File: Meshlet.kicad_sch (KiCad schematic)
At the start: 99 parts, among them J11 GPIO Exp., J12 GPS Header, J13 Thermistor Pins, J14 Ext. Notif. Header, J2 User Btn Header, J3 Batt. Header (Picoblade 1.25), J4 Batt. Header (JST-PH 2.0), J5 USB_C_Receptacle_USB2.0_16P, J6 STEMMA QT I2C, J7 Ext. Power Header, J9 Ext. Power Header, Q1 AO3400A, SW2 BOOTSEL, U1 XC6206PxxxMR, U11 INA3221, U2 USBLC6-2SC6, U3 XC6206PxxxMR, U4 RP2350_60QFN, U5 Wio-SX1262, U6 BQ25185, U7 BME280, U8 W25Q32JVZP, U9 XC6206PxxxMR, Y1 12.000MHz

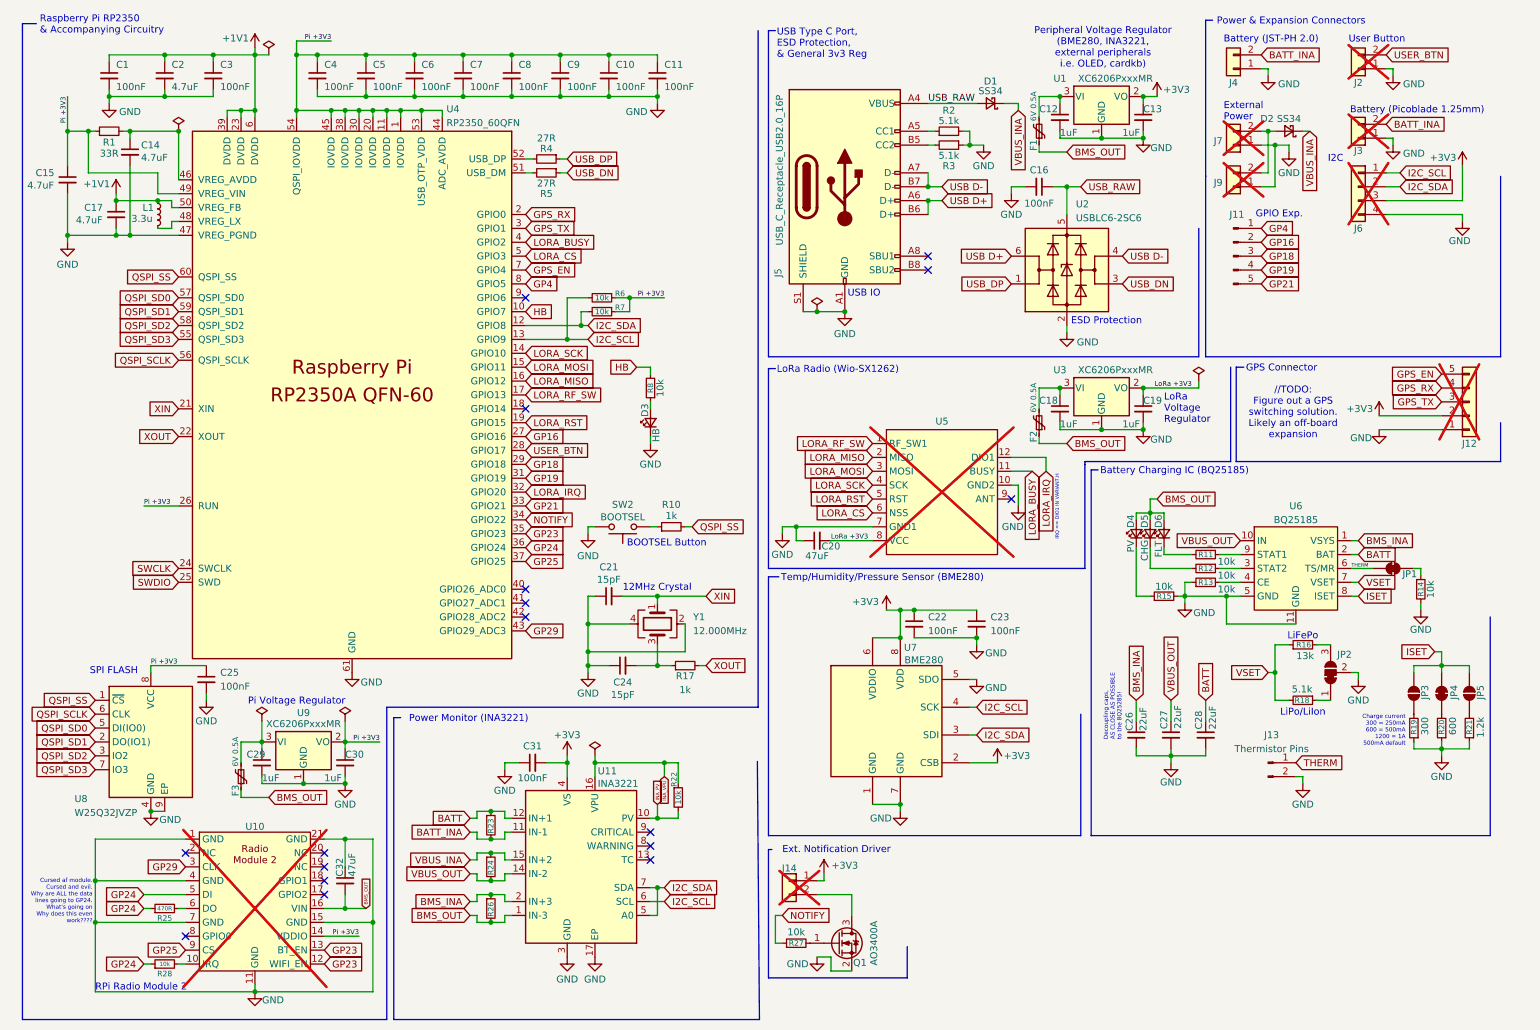
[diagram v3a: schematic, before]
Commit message: Add GPS header
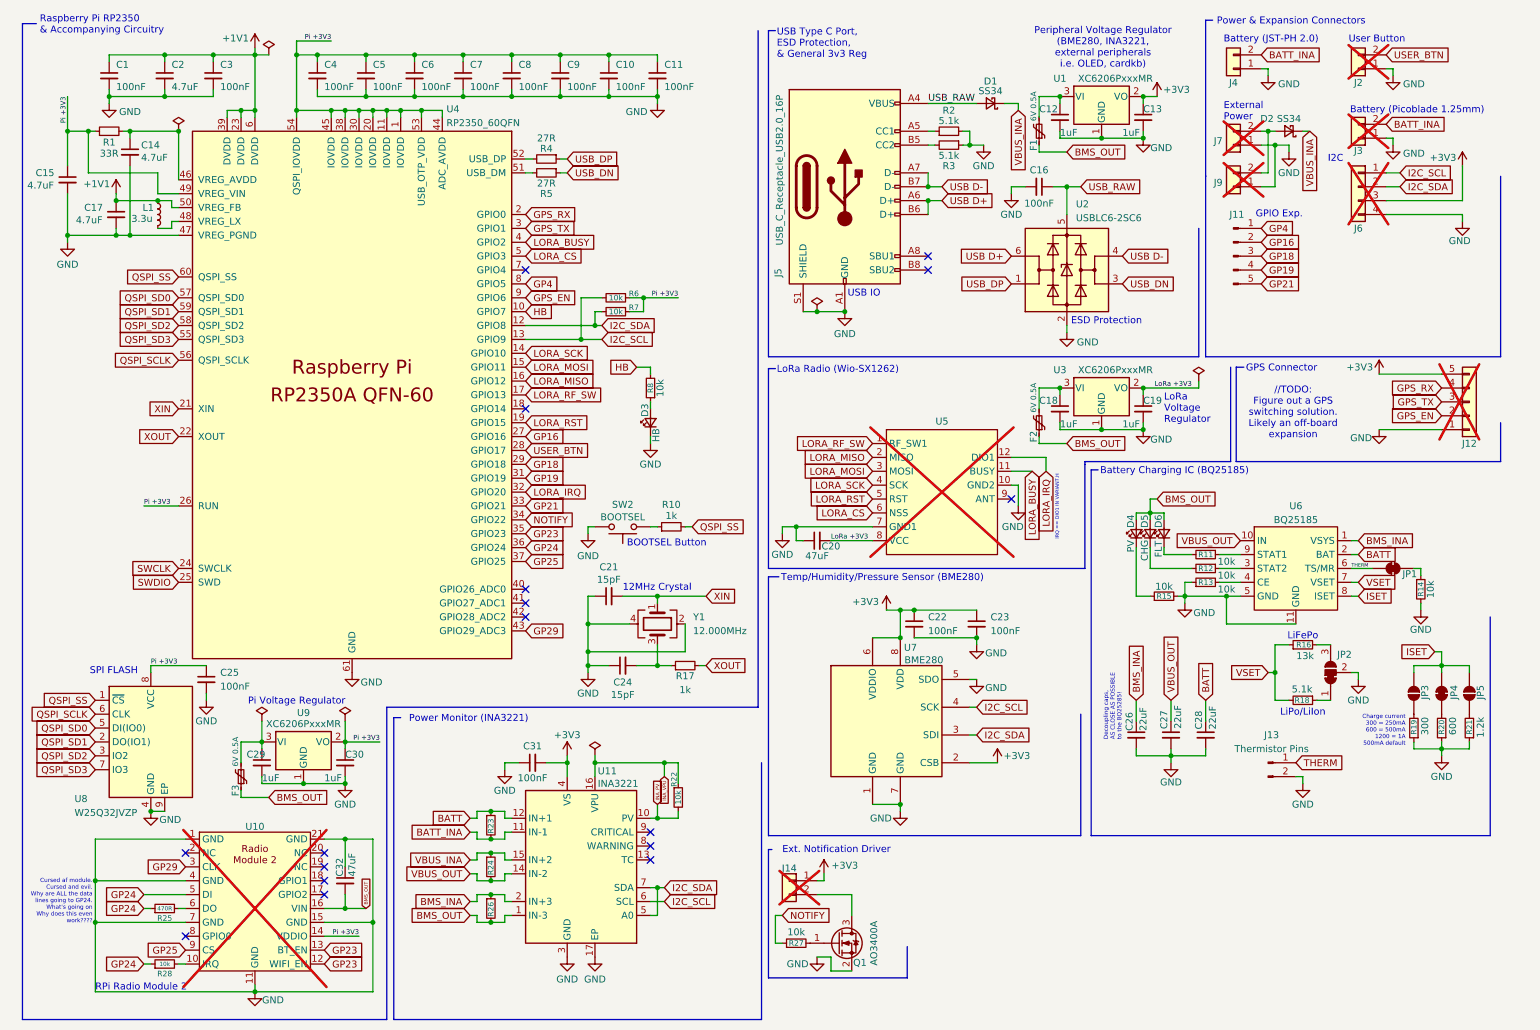
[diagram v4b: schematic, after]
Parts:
- J12: footprint Connector_PinHeader_2.00mm:PinHeader_1x05_P2.00mm_Vertical -> Connector_PinHeader_1.27mm:PinHeader_1x05_P1.27mm_Vertical
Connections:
- net +3V3: now also J12.5 (Pin_5); no longer J12.2 (Pin_2)
- net GPS_EN: now also J12.2 (Pin_2), U4.9 (GPIO6); no longer J12.5 (Pin_5), U4.7 (GPIO4)
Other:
- moved on the sheet: R6, R7
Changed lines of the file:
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@@
 	)
 	(junction
+		(at 118.11 69.85)
+		(diameter 0)
+		(color 0 0 0 0)
+	)
+	(junction
 		(at 21.59 34.29)
 		(diameter 0)
@@
 	)
 	(junction
-		(at 115.57 69.85)
-		(diameter 0)
-		(color 0 0 0 0)
-	)
-	(junction
 		(at 210.82 88.9)
 		(diameter 0)
@@
 	)
 	(junction
-		(at 124.46 64.77)
+		(at 127 64.77)
 		(diameter 0)
 		(color 0 0 0 0)
@@
 	)
 	(junction
+		(at 115.57 72.39)
+		(diameter 0)
+		(color 0 0 0 0)
+	)
+	(junction
 		(at 39.37 20.32)
 		(diameter 0)
@@
 		(color 0 0 0 0)
 	)
-	(junction
-		(at 113.03 72.39)
-		(diameter 0)
-		(color 0 0 0 0)
-	)
 	(no_connect
 		(at 105.41 123.19)
 	)
 	(no_connect
-		(at 105.41 64.77)
-	)
-	(no_connect
 		(at 105.41 118.11)
 	)
@@
 	)
 	(no_connect
+		(at 105.41 59.69)
+	)
+	(no_connect
 		(at 43.18 181.61)
 	)
@@
 	(wire
 		(pts
-			(xy 115.57 69.85) (xy 116.84 69.85)
-		)
-		(stroke
-			(width 0)
-			(type default)
-		)
-	)
-	(wire
-		(pts
-			(xy 105.41 72.39) (xy 113.03 72.39)
+			(xy 105.41 72.39) (xy 115.57 72.39)
 		)
 		(stroke
@@
 	(polyline
 		(pts
-			(xy 147.828 149.606) (xy 148.209 196.85)
+			(xy 148.59 149.86) (xy 148.59 196.85)
 		)
 		(stroke
@@
 		)
 	)
+	(wire
+		(pts
+			(xy 115.57 72.39) (xy 119.38 72.39)
+		)
+		(stroke
+			(width 0)
+			(type default)
+		)
+	)
 	(polyline
 		(pts
@@
 	(wire
 		(pts
-			(xy 121.92 67.31) (xy 124.46 67.31)
+			(xy 124.46 67.31) (xy 127 67.31)
 		)
 		(stroke
@@
 	(wire
 		(pts
-			(xy 261.62 86.36) (xy 273.05 86.36)
+			(xy 261.62 78.74) (xy 273.05 78.74)
 		)
 		(stroke
@@
 	(wire
 		(pts
-			(xy 105.41 69.85) (xy 115.57 69.85)
+			(xy 105.41 69.85) (xy 118.11 69.85)
 		)
 		(stroke
@@
 	(wire
 		(pts
-			(xy 116.84 67.31) (xy 115.57 67.31)
+			(xy 119.38 67.31) (xy 118.11 67.31)
 		)
 		(stroke
@@
 	(wire
 		(pts
-			(xy 115.57 67.31) (xy 115.57 69.85)
+			(xy 118.11 67.31) (xy 118.11 69.85)
 		)
 		(stroke
@@
 	(wire
 		(pts
-			(xy 116.84 64.77) (xy 113.03 64.77)
+			(xy 119.38 64.77) (xy 115.57 64.77)
 		)
 		(stroke
@@
 	(wire
 		(pts
+			(xy 118.11 69.85) (xy 119.38 69.85)
+		)
+		(stroke
+			(width 0)
+			(type default)
+		)
+	)
+	(wire
+		(pts
 			(xy 176.53 127) (xy 187.96 127)
 		)
@@
 	(wire
 		(pts
-			(xy 124.46 64.77) (xy 130.81 64.77)
+			(xy 127 64.77) (xy 133.35 64.77)
 		)
 		(stroke
@@
 	(wire
 		(pts
-			(xy 121.92 64.77) (xy 124.46 64.77)
+			(xy 124.46 64.77) (xy 127 64.77)
 		)
 		(stroke
@@
 	(polyline
 		(pts
-			(xy 81.28 196.85) (xy 148.209 196.85)
+			(xy 81.28 196.85) (xy 148.59 196.85)
 		)
 		(stroke
@@
 	(wire
 		(pts
-			(xy 124.46 67.31) (xy 124.46 64.77)
+			(xy 127 67.31) (xy 127 64.77)
 		)
 		(stroke
@@
 	(wire
 		(pts
-			(xy 113.03 64.77) (xy 113.03 72.39)
+			(xy 115.57 64.77) (xy 115.57 72.39)
 		)
 		(stroke
@@
 	(wire
 		(pts
-			(xy 113.03 72.39) (xy 116.84 72.39)
-		)
-		(stroke
-			(width 0)
-			(type default)
-		)
-	)
-	(wire
-		(pts
 			(xy 99.06 173.99) (xy 101.6 173.99)
 		)
@@
 	)
 	(label "Pi +3V3"
-		(at 130.81 64.77 180)
+		(at 133.35 64.77 180)
 		(effects
 			(font
@@
 	(global_label "GPS_EN"
 		(shape input)
-		(at 273.05 78.74 180)
+		(at 273.05 86.36 180)
 		(fields_autoplaced yes)
 		(effects
@@
 		)
 		(property "Intersheetrefs" "${INTERSHEET_REFS}"
-			(at 262.8682 78.74 0)
+			(at 262.8682 86.36 0)
 			(effects
 				(font
@@
 	(global_label "I2C_SDA"
 		(shape input)
-		(at 116.84 69.85 0)
+		(at 119.38 69.85 0)
 		(fields_autoplaced yes)
 		(effects
@@
 		)
 		(property "Intersheetrefs" "${INTERSHEET_REFS}"
-			(at 127.4452 69.85 0)
+			(at 129.9852 69.85 0)
 			(effects
 				(font
@@
 	(global_label "I2C_SCL"
 		(shape input)
-		(at 116.84 72.39 0)
+		(at 119.38 72.39 0)
 		(fields_autoplaced yes)
 		(effects
@@
 		)
 		(property "Intersheetrefs" "${INTERSHEET_REFS}"
-			(at 127.3847 72.39 0)
+			(at 129.9247 72.39 0)
 			(effects
 				(font
@@
 	(global_label "GPS_EN"
 		(shape input)
-		(at 105.41 59.69 0)
+		(at 105.41 64.77 0)
 		(fields_autoplaced yes)
 		(effects
@@
 		)
 		(property "Intersheetrefs" "${INTERSHEET_REFS}"
-			(at 112.1447 59.69 0)
+			(at 112.1447 64.77 0)
 			(effects
 				(font
@@
 			)
 		)
-		(property "Footprint" "Connector_PinHeader_2.00mm:PinHeader_1x05_P2.00mm_Vertical"
+		(property "Footprint" "Connector_PinHeader_1.27mm:PinHeader_1x05_P1.27mm_Vertical"
 			(at 278.13 83.82 0)
 			(effects
@@
 		(lib_name "R_Small_6")
 		(lib_id "Device:R_Small")
-		(at 119.38 67.31 270)
+		(at 121.92 67.31 270)
 		(unit 1)
 		(exclude_from_sim no)
@@
 		(dnp no)
 		(property "Reference" "R7"
-			(at 122.682 66.548 90)
+			(at 125.222 66.548 90)
 			(effects
 				(font
@@
 		)
 		(property "Value" "10k"
-			(at 119.38 67.31 90)
+			(at 121.92 67.31 90)
 			(effects
 				(font
@@
 		)
 		(property "Footprint" "Resistor_SMD:R_0402_1005Metric"
-			(at 119.38 67.31 0)
+			(at 121.92 67.31 0)
 			(effects
 				(font
@@
 		)
 		(property "Datasheet" "~"
-			(at 119.38 67.31 0)
+			(at 121.92 67.31 0)
 			(effects
 				(font
@@
 		)
 		(property "Description" "Resistor, small symbol"
-			(at 119.38 67.31 0)
+			(at 121.92 67.31 0)
 			(effects
 				(font
@@
 		)
 		(property "LCSC" "C25744"
-			(at 119.38 67.31 90)
+			(at 121.92 67.31 90)
 			(effects
 				(font
@@
 		(lib_name "R_Small_6")
 		(lib_id "Device:R_Small")
-		(at 119.38 64.77 270)
+		(at 121.92 64.77 270)
 		(unit 1)
 		(exclude_from_sim no)
@@
 		(dnp no)
 		(property "Reference" "R6"
-			(at 122.682 64.008 90)
+			(at 125.222 64.008 90)
 			(effects
 				(font
@@
 		)
 		(property "Value" "10k"
-			(at 119.38 64.77 90)
+			(at 121.92 64.77 90)
 			(effects
 				(font
@@
 		)
 		(property "Footprint" "Resistor_SMD:R_0402_1005Metric"
-			(at 119.38 64.77 0)
+			(at 121.92 64.77 0)
 			(effects
 				(font
@@
 		)
 		(property "Datasheet" "~"
-			(at 119.38 64.77 0)
+			(at 121.92 64.77 0)
 			(effects
 				(font
@@
 		)
 		(property "Description" "Resistor, small symbol"
-			(at 119.38 64.77 0)
+			(at 121.92 64.77 0)
 			(effects
 				(font
@@
 		)
 		(property "LCSC" "C25744"
-			(at 119.38 64.77 90)
+			(at 121.92 64.77 90)
 			(effects
 				(font
@@
 	(symbol
 		(lib_id "power:+3V3")
-		(at 261.62 86.36 0)
+		(at 261.62 78.74 0)
 		(unit 1)
 		(exclude_from_sim no)
@@
 		(dnp no)
 		(property "Reference" "#PWR023"
-			(at 261.62 90.17 0)
+			(at 261.62 82.55 0)
 			(effects
 				(font
@@
 		)
 		(property "Value" "+3V3"
-			(at 258.064 85.09 0)
+			(at 258.064 77.47 0)
 			(effects
 				(font
@@
 		)
 		(property "Footprint" ""
-			(at 261.62 86.36 0)
+			(at 261.62 78.74 0)
 			(effects
 				(font
@@
 		)
 		(property "Datasheet" ""
-			(at 261.62 86.36 0)
+			(at 261.62 78.74 0)
 			(effects
 				(font
@@
 		)
 		(property "Description" "Power symbol creates a global label with name \"+3V3\""
-			(at 261.62 86.36 0)
+			(at 261.62 78.74 0)
 			(effects
 				(font

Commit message: Add test points for power
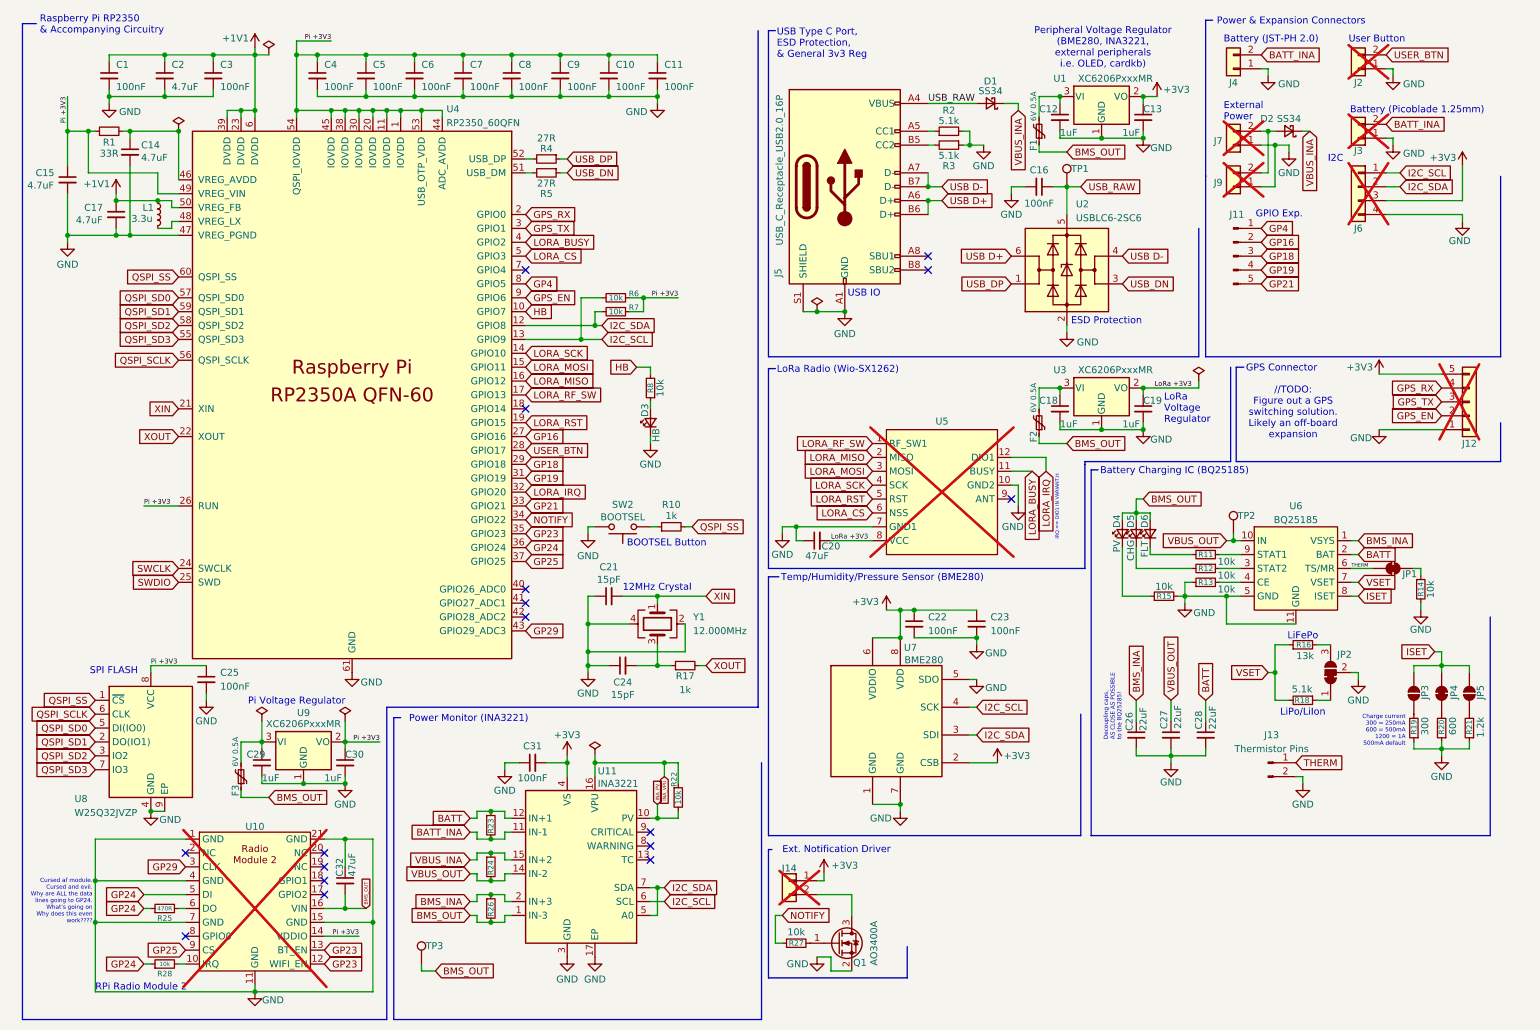
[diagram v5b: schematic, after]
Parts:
- added TP1, TP2, TP3: TestPoint, TestPoint:TestPoint_Pad_D1.0mm, symbol Connector:TestPoint
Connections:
- net BMS_OUT: now also TP3.1
- net USB_RAW: now also TP1.1
- net VBUS_OUT: now also TP2.1
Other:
- moved on the sheet: D4, D5, D6
